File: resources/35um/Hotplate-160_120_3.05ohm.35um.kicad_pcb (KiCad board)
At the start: 2 copper layers, 100 x 100 mm, 7 parts, among them J1 Hotplate_Power_Connection, J2 Hotplate_Power_Connection

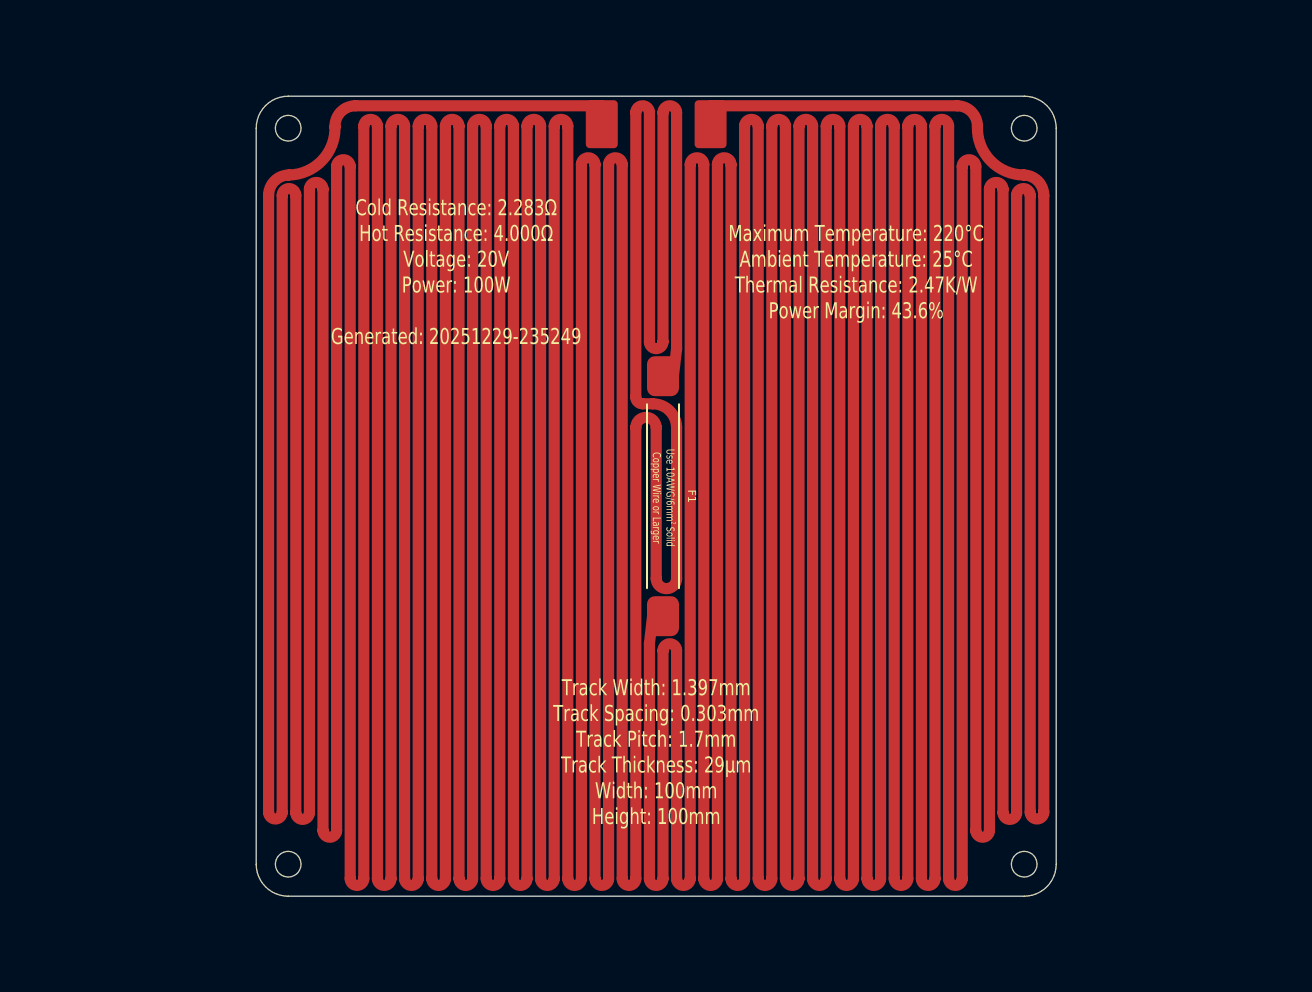
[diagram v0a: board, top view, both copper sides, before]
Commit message: Replaced obsolete 25mm thermal fuse footprint with new 35mm thermal fuse footprint.
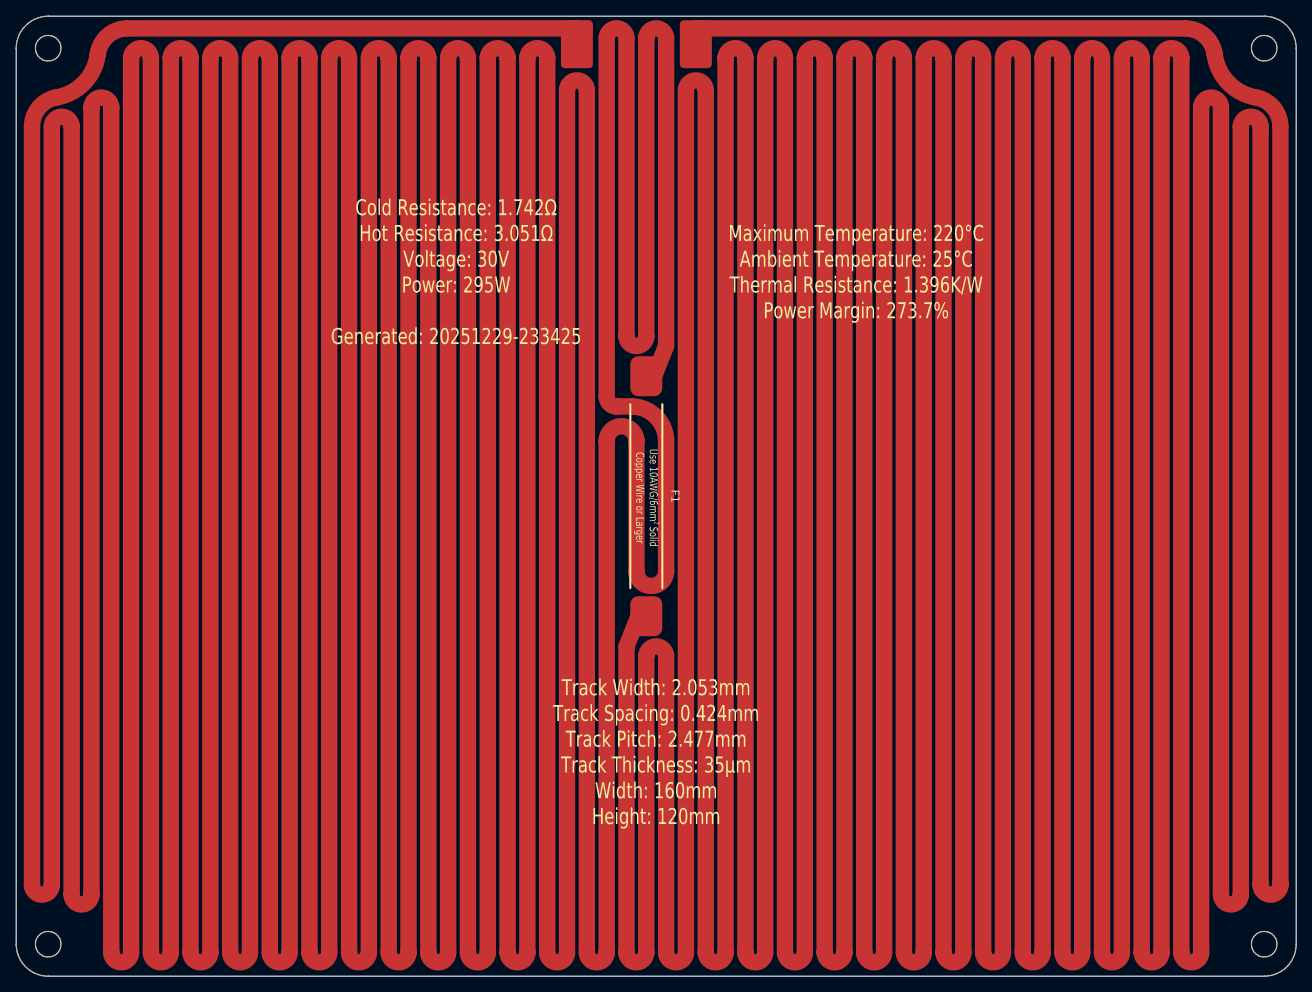
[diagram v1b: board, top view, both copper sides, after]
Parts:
- moved REF** 31.6 mm to (181.0, 49.0)
- moved REF** 31.6 mm to (29.0, 161.0)
- moved REF** 31.6 mm to (181.0, 161.0)
- moved REF** 31.6 mm to (29.0, 49.0)
- moved J1 10.5 mm to (95.1, 48.5)
- moved J2 10.2 mm to (110.0, 48.5)
- moved F1 2.09 mm to (103.8, 105.0)
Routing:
- net Net-(J2-Pin_1): track 2634.1 -> 3702.0 mm
- net Net-(J1-Pin_1): track 2780.9 -> 3632.7 mm
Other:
- board size 100 x 100 mm -> 160 x 120 mm
- board text added: "Cold Resistance: 1.742Ω Hot Resistance: 3.051Ω Voltage: 30V Power: 295W Generated: 20251229-233425"
- board text added: "Maximum Temperature: 220°C Ambient Temperature: 25°C Thermal Resistance: 1.396K/W Power Margin: 273.7%"
- board text added: "Track Width: 2.053mm Track Spacing: 0.424mm Track Pitch: 2.477mm Track Thickness: 35µm Width: 160mm Height: 120mm"
- board text removed: "Cold Resistance: 2.283Ω Hot Resistance: 4.000Ω Voltage: 20V Power: 100W Generated: 20251229-235249"
- board text removed: "Maximum Temperature: 220°C Ambient Temperature: 25°C Thermal Resistance: 2.47K/W Power Margin: 43.6%"
- board text removed: "Track Width: 1.397mm Track Spacing: 0.303mm Track Pitch: 1.7mm Track Thickness: 29µm Width: 100mm Height: 100mm"
